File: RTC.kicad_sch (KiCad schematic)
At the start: 5 parts, among them U2 MCP795W22-I/ST, Y1 TG-3541CE

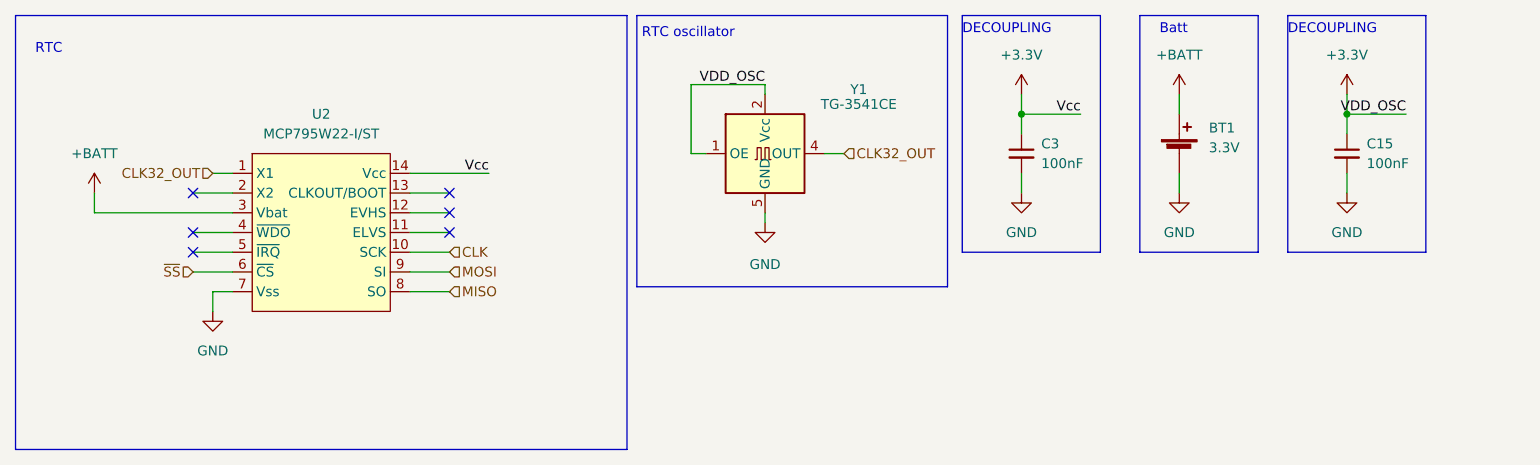
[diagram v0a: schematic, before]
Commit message: V1
- Corrected SD-cards footprint and schematical represantation;
- Corrected RTC shematics:
	- changed oscilators power supply from internal 3v3 to Vbat so RTC works when PCB is disconnected from external power supply [PWR PCB];
	- 32 kHz to microcontroller now comes from RTC module;
	- added 100 nF decoupling capacitor to Vbat RTC pin.
- Corrected couple connections and component placement on PCB
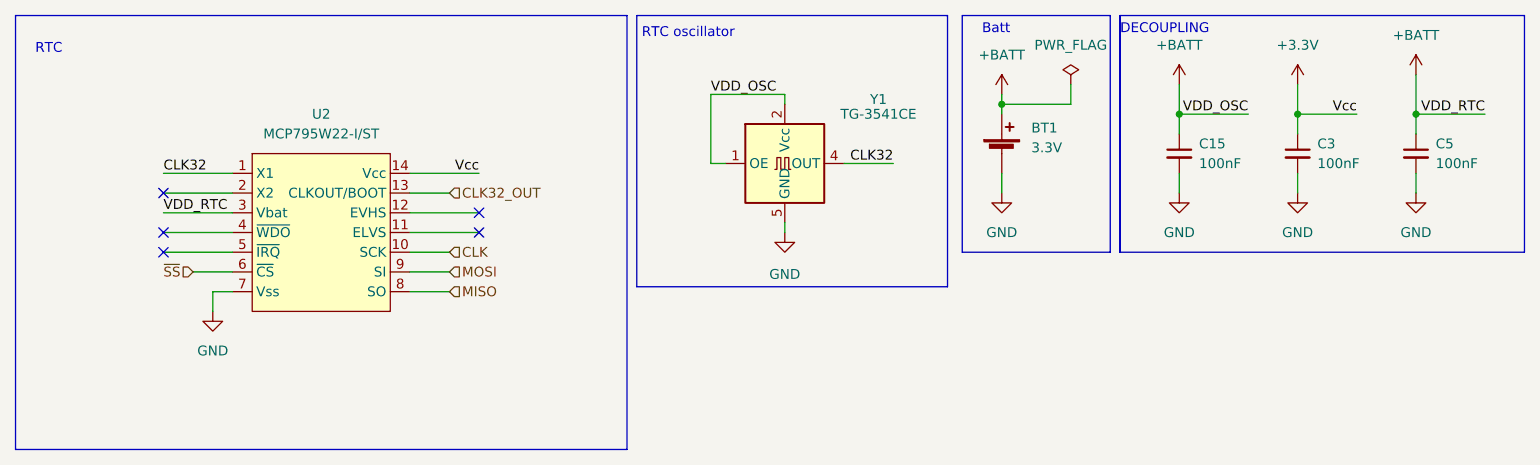
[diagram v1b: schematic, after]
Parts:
- added C5: 100nF, Capacitor_SMD:C_0402_1005Metric, symbol Device:C_Small
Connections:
- net +3V3: no longer C15.1, Y1.1 (OE), Y1.2 (Vcc), Y1.3 (Vcc)
- net +BATT: now also C15.1, Y1.1 (OE), Y1.2 (Vcc), Y1.3 (Vcc), C5.1
- net CLK32_OUT: now also U2.13 (CLKOUT/BOOT); no longer U2.1 (X1), Y1.4 (OUT)
- net GND: now also C5.2
- new net CLK32: U2.1 (X1), Y1.4 (OUT)
- no-connect marks 6 -> 5
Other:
- company: (none) -> BASEMENT
- moved on the sheet: BT1, C15, C3, Y1
